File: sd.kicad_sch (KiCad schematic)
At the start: 40 parts, among them Y1 ABM8G-24.000MHZ-18-D2Y-T

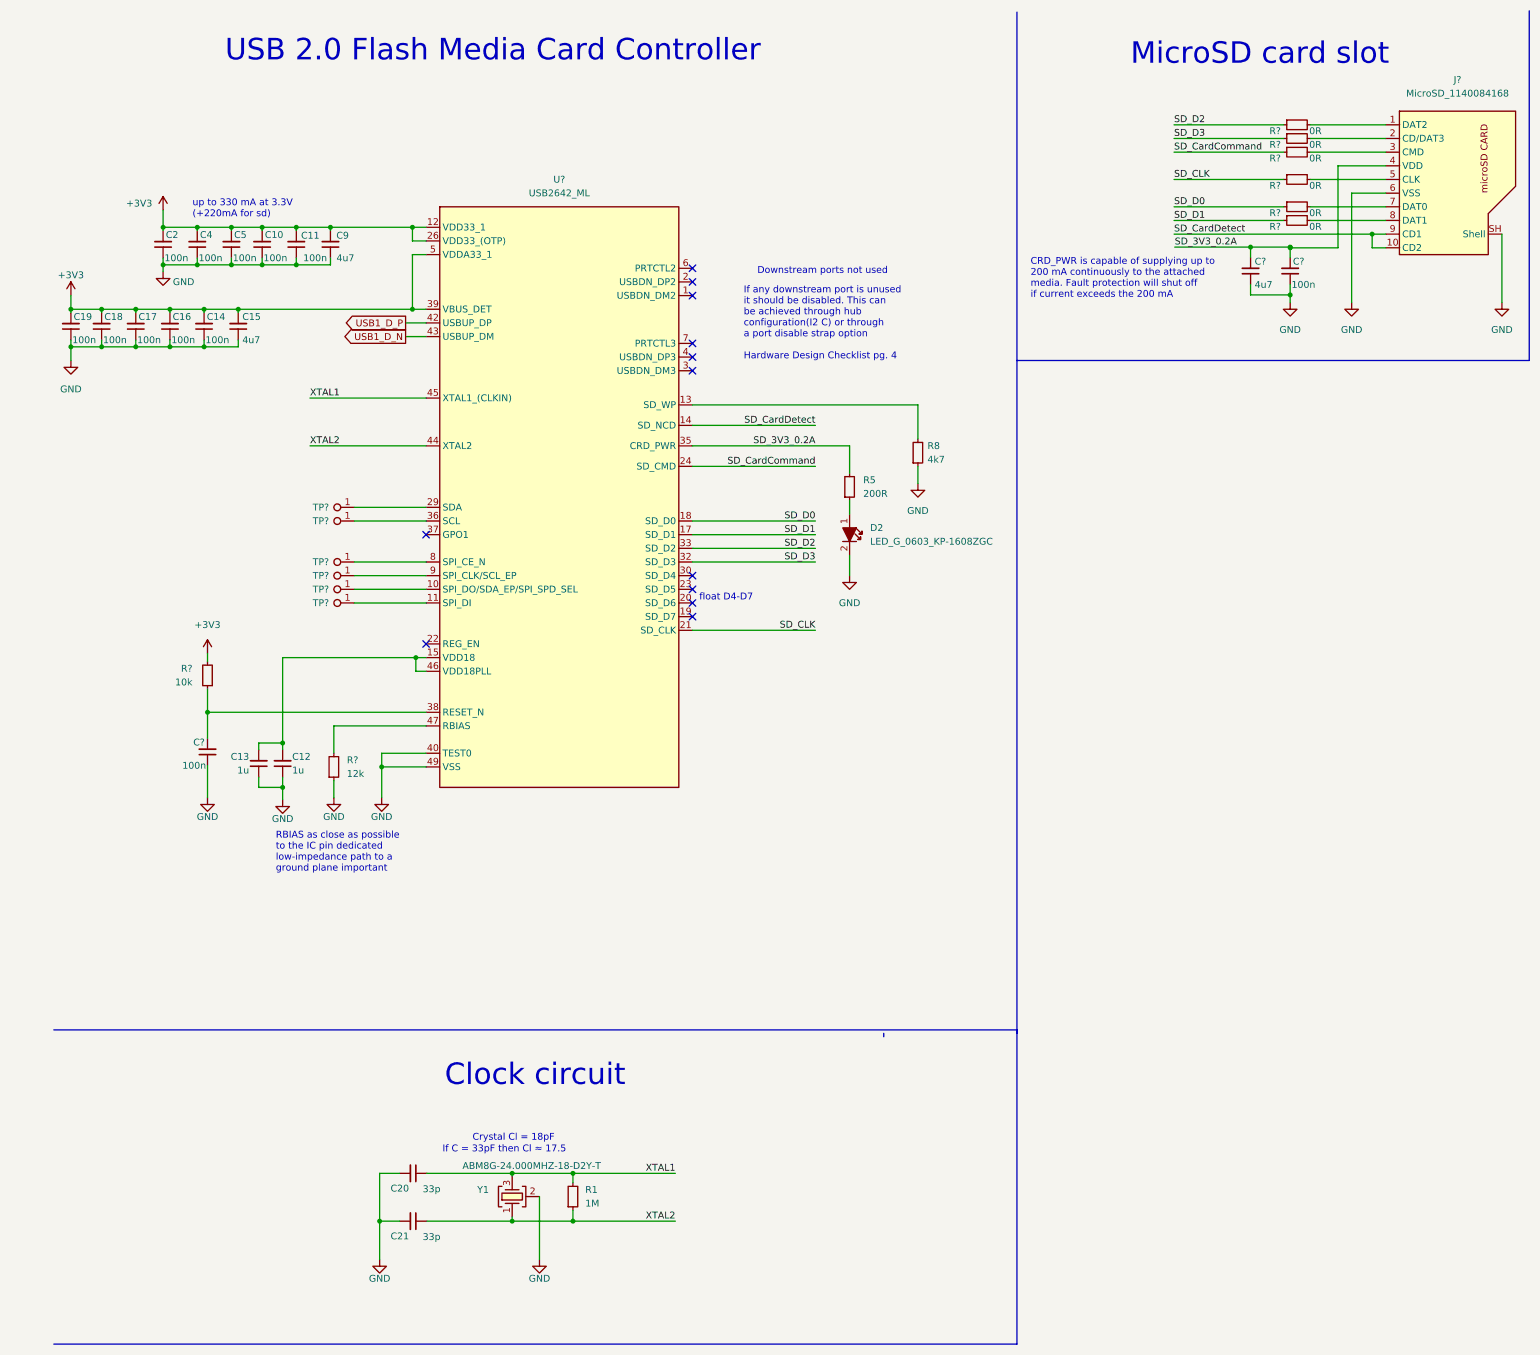
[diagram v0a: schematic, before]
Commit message: [#45990] Route dif Pcie, place susclk gen
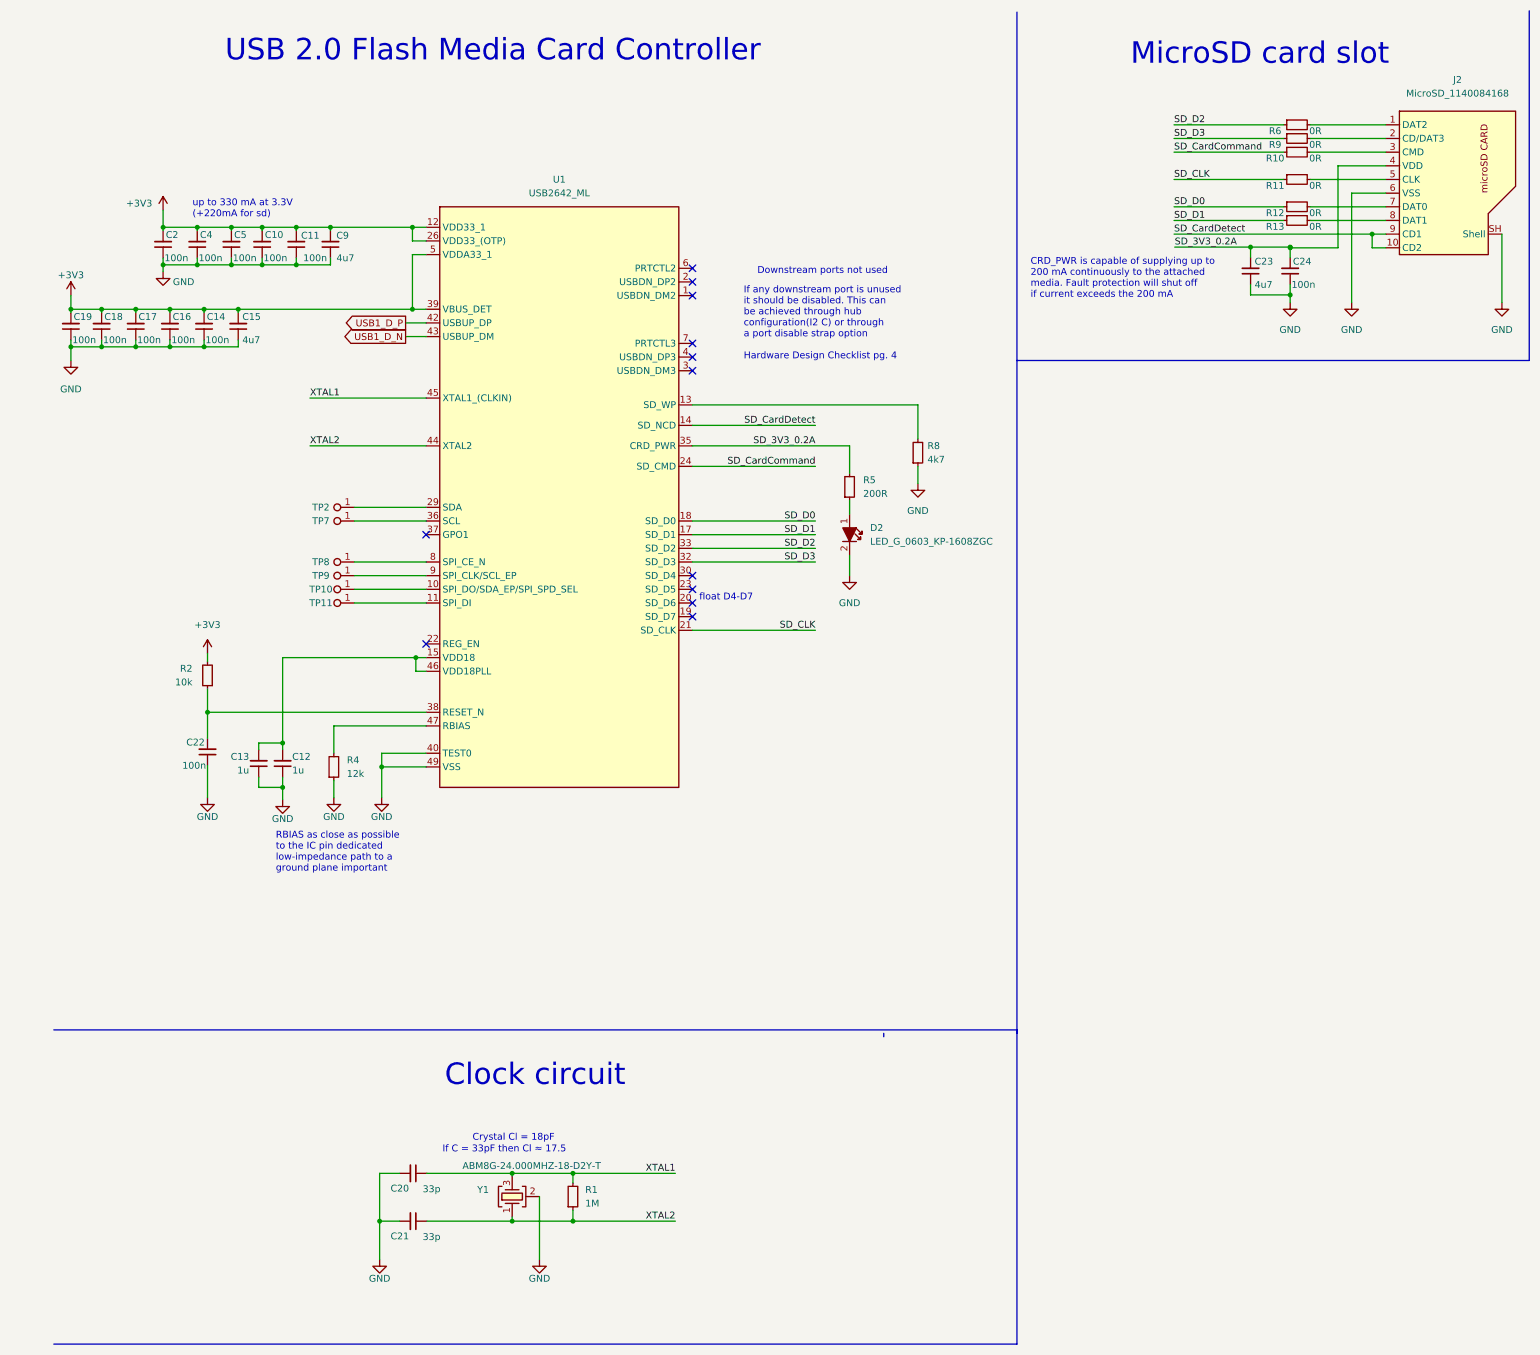
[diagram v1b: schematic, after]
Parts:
- gave numbers to parts that had none: 19
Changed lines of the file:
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@@
   (symbol (lib_id "antmicroResistors0603:R_0R_0603") (at 240.665 43.18 0) (unit 1)
     (in_bom yes) (on_board yes)
-    (property "Reference" "R?" (id 0) (at 239.141 44.323 0)
+    (property "Reference" "R11" (id 0) (at 239.141 44.323 0)
       (effects (font (size 1.27 1.27) (thickness 0.15)))
     )
@@
   (symbol (lib_id "antmicroResistors0402:R_10k_0402") (at 40.64 137.922 270) (mirror x) (unit 1)
     (in_bom yes) (on_board yes) (fields_autoplaced)
-    (property "Reference" "R?" (id 0) (at 37.846 134.1119 90)
+    (property "Reference" "R2" (id 0) (at 37.846 134.1119 90)
       (effects (font (size 1.27 1.27) (thickness 0.15)) (justify right))
     )
@@
   (symbol (lib_id "antmicroTestPoints:TP_0.75mm_SMD") (at 67.945 104.14 180) (unit 1)
     (in_bom yes) (on_board yes)
-    (property "Reference" "TP?" (id 0) (at 61.722 104.14 0)
+    (property "Reference" "TP2" (id 0) (at 61.722 104.14 0)
       (effects (font (size 1.27 1.27) (thickness 0.15)))
     )
@@
   (symbol (lib_id "antmicroTestPoints:TP_0.75mm_SMD") (at 67.945 114.3 180) (unit 1)
     (in_bom yes) (on_board yes)
-    (property "Reference" "TP?" (id 0) (at 61.722 114.3 0)
+    (property "Reference" "TP8" (id 0) (at 61.722 114.3 0)
       (effects (font (size 1.27 1.27) (thickness 0.15)))
     )
@@
   (symbol (lib_id "antmicroResistors0603:R_0R_0603") (at 240.665 35.56 0) (unit 1)
     (in_bom yes) (on_board yes)
-    (property "Reference" "R?" (id 0) (at 239.141 36.703 0)
+    (property "Reference" "R9" (id 0) (at 239.141 36.703 0)
       (effects (font (size 1.27 1.27) (thickness 0.15)))
     )
@@
   (symbol (lib_id "antmicroTestPoints:TP_0.75mm_SMD") (at 67.945 121.92 180) (unit 1)
     (in_bom yes) (on_board yes)
-    (property "Reference" "TP?" (id 0) (at 61.722 121.92 0)
+    (property "Reference" "TP11" (id 0) (at 61.722 121.92 0)
       (effects (font (size 1.27 1.27) (thickness 0.15)))
     )
@@
   (symbol (lib_id "antmicroCapacitors0402:C_100n_0402") (at 40.64 152.146 270) (mirror x) (unit 1)
     (in_bom yes) (on_board yes)
-    (property "Reference" "C?" (id 0) (at 40.132 147.828 90)
+    (property "Reference" "C22" (id 0) (at 40.132 147.828 90)
       (effects (font (size 1.27 1.27) (thickness 0.15)) (justify right))
     )
@@
   (symbol (lib_id "antmicroCapacitors0402:C_100n_0402") (at 241.935 62.738 90) (unit 1)
     (in_bom yes) (on_board yes)
-    (property "Reference" "C?" (id 0) (at 242.443 58.42 90)
+    (property "Reference" "C24" (id 0) (at 242.443 58.42 90)
       (effects (font (size 1.27 1.27) (thickness 0.15)) (justify right))
     )
@@
   (symbol (lib_id "antmicroResistors0603:R_0R_0603") (at 240.665 33.02 0) (unit 1)
     (in_bom yes) (on_board yes)
-    (property "Reference" "R?" (id 0) (at 239.141 34.163 0)
+    (property "Reference" "R6" (id 0) (at 239.141 34.163 0)
       (effects (font (size 1.27 1.27) (thickness 0.15)))
     )
@@
   (symbol (lib_id "antmicroTestPoints:TP_0.75mm_SMD") (at 67.945 106.68 180) (unit 1)
     (in_bom yes) (on_board yes)
-    (property "Reference" "TP?" (id 0) (at 61.722 106.68 0)
+    (property "Reference" "TP7" (id 0) (at 61.722 106.68 0)
       (effects (font (size 1.27 1.27) (thickness 0.15)))
     )
@@
   (symbol (lib_id "antmicropower:GND") (at 253.365 66.04 0) (unit 1)
     (in_bom yes) (on_board yes) (fields_autoplaced)
-    (property "Reference" "#PWR?" (id 0) (at 253.365 72.39 0)
+    (property "Reference" "#PWR0115" (id 0) (at 253.365 72.39 0)
       (effects (font (size 1.27 1.27)) hide)
     )
@@
   (symbol (lib_id "antmicropower:GND") (at 40.64 158.115 0) (mirror y) (unit 1)
     (in_bom yes) (on_board yes)
-    (property "Reference" "#PWR?" (id 0) (at 40.64 164.465 0)
+    (property "Reference" "#PWR0112" (id 0) (at 40.64 164.465 0)
       (effects (font (size 1.27 1.27)) hide)
     )
@@
   (symbol (lib_id "antmicroMemoryConnectorsPCCardSockets:MicroSD_1140084168") (at 259.715 33.02 0) (unit 1)
     (in_bom yes) (on_board yes) (fields_autoplaced)
-    (property "Reference" "J?" (id 0) (at 273.05 24.638 0)
+    (property "Reference" "J2" (id 0) (at 273.05 24.638 0)
       (effects (font (size 1.27 1.27) (thickness 0.15)))
     )
@@
   (symbol (lib_id "antmicroResistors0603:R_0R_0603") (at 240.665 48.26 0) (unit 1)
     (in_bom yes) (on_board yes)
-    (property "Reference" "R?" (id 0) (at 239.141 49.403 0)
+    (property "Reference" "R12" (id 0) (at 239.141 49.403 0)
       (effects (font (size 1.27 1.27) (thickness 0.15)))
     )
@@
   (symbol (lib_id "antmicroInterfaceControllers:USB2642_ML") (at 130.81 46.99 0) (unit 1)
     (in_bom yes) (on_board yes) (fields_autoplaced)
-    (property "Reference" "U?" (id 0) (at 106.045 43.18 0)
+    (property "Reference" "U1" (id 0) (at 106.045 43.18 0)
       (effects (font (size 1.27 1.27) (thickness 0.15)))
     )
@@
   (symbol (lib_id "antmicropower:+3V3") (at 40.64 131.318 0) (unit 1)
     (in_bom yes) (on_board yes) (fields_autoplaced)
-    (property "Reference" "#PWR?" (id 0) (at 40.64 135.128 0)
+    (property "Reference" "#PWR0113" (id 0) (at 40.64 135.128 0)
       (effects (font (size 1.27 1.27)) hide)
     )
@@
   (symbol (lib_id "antmicroTestPoints:TP_0.75mm_SMD") (at 67.945 119.38 180) (unit 1)
     (in_bom yes) (on_board yes)
-    (property "Reference" "TP?" (id 0) (at 61.722 119.38 0)
+    (property "Reference" "TP10" (id 0) (at 61.722 119.38 0)
       (effects (font (size 1.27 1.27) (thickness 0.15)))
     )
@@
   (symbol (lib_id "antmicroResistorsmisc:R_12k_0805") (at 64.135 154.94 90) (unit 1)
     (in_bom yes) (on_board yes) (fields_autoplaced)
-    (property "Reference" "R?" (id 0) (at 66.548 151.1299 90)
+    (property "Reference" "R4" (id 0) (at 66.548 151.1299 90)
       (effects (font (size 1.27 1.27) (thickness 0.15)) (justify right))
     )
@@
   (symbol (lib_id "antmicropower:GND") (at 241.935 66.04 0) (unit 1)
     (in_bom yes) (on_board yes) (fields_autoplaced)
-    (property "Reference" "#PWR?" (id 0) (at 241.935 72.39 0)
+    (property "Reference" "#PWR0117" (id 0) (at 241.935 72.39 0)
       (effects (font (size 1.27 1.27)) hide)
     )
@@
   (symbol (lib_id "antmicroResistors0603:R_0R_0603") (at 240.665 38.1 0) (unit 1)
     (in_bom yes) (on_board yes)
-    (property "Reference" "R?" (id 0) (at 239.141 39.243 0)
+    (property "Reference" "R10" (id 0) (at 239.141 39.243 0)
       (effects (font (size 1.27 1.27) (thickness 0.15)))
     )
@@
   (symbol (lib_id "antmicropower:GND") (at 64.135 158.115 0) (mirror y) (unit 1)
     (in_bom yes) (on_board yes)
-    (property "Reference" "#PWR?" (id 0) (at 64.135 164.465 0)
+    (property "Reference" "#PWR0109" (id 0) (at 64.135 164.465 0)
       (effects (font (size 1.27 1.27)) hide)
     )
@@
   (symbol (lib_id "antmicroCapacitors0402:C_4u7_0402") (at 234.569 62.738 90) (unit 1)
     (in_bom yes) (on_board yes)
-    (property "Reference" "C?" (id 0) (at 235.331 58.42 90)
+    (property "Reference" "C23" (id 0) (at 235.331 58.42 90)
       (effects (font (size 1.27 1.27) (thickness 0.15)) (justify right))
     )
@@
   (symbol (lib_id "antmicroTestPoints:TP_0.75mm_SMD") (at 67.945 116.84 180) (unit 1)
     (in_bom yes) (on_board yes)
-    (property "Reference" "TP?" (id 0) (at 61.722 116.84 0)
+    (property "Reference" "TP9" (id 0) (at 61.722 116.84 0)
       (effects (font (size 1.27 1.27) (thickness 0.15)))
     )
@@
   (symbol (lib_id "antmicroResistors0603:R_0R_0603") (at 240.665 50.8 0) (unit 1)
     (in_bom yes) (on_board yes)
-    (property "Reference" "R?" (id 0) (at 239.141 51.943 0)
-      (effects (font (size 1.27 1.27) (thickness 0.15)))
-    )
+    (property "Reference" "R13" (id 0) (at 239.141 51.943 0)
+      (effects (font (size 1.27 1.27) (thickness 0.15)))
+    )

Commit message: [#45990] Fix silk screen drcs
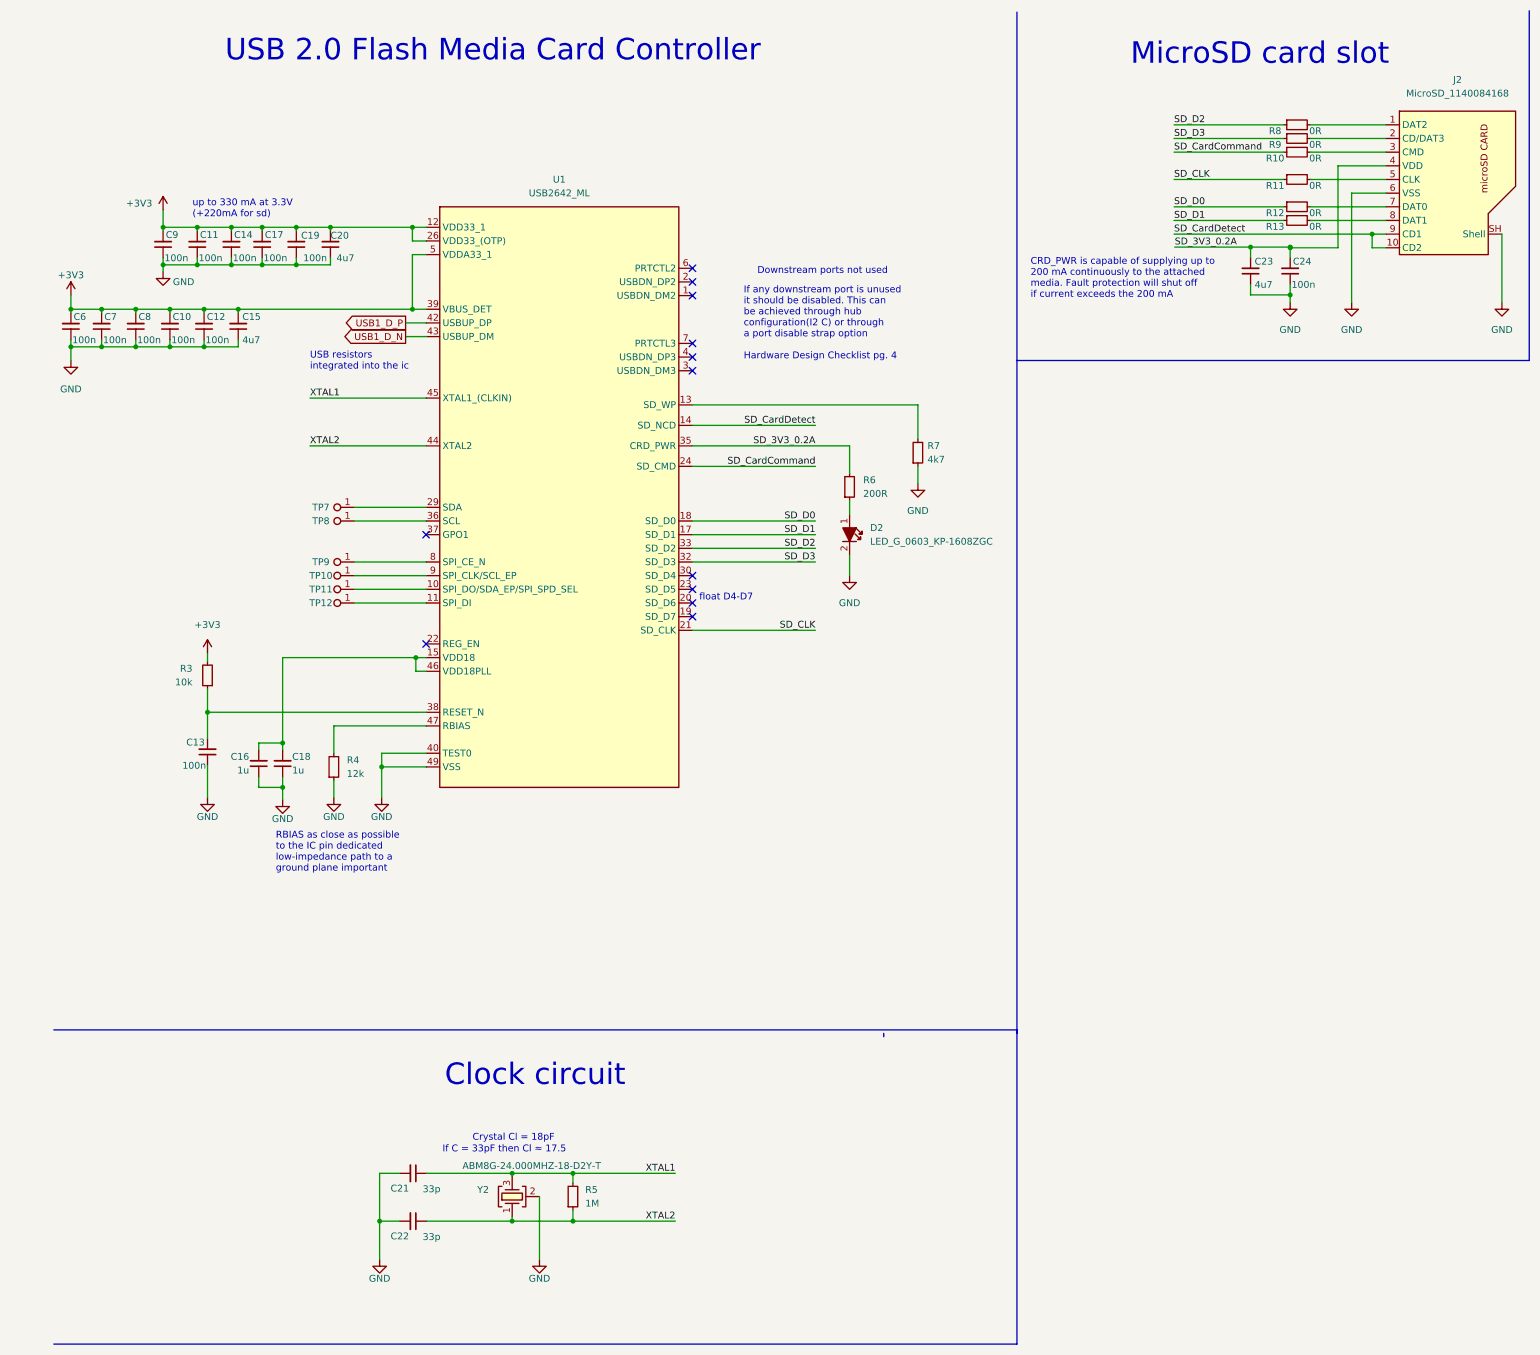
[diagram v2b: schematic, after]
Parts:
- renumbered C16 to C10, C4 to C11, C14 to C12, C22 to C13, C5 to C14, C13 to C16, C10 to C17, C12 to C18, C11 to C19, C9 to C20, C20 to C21, C21 to C22, C19 to C6, C18 to C7, C17 to C8, C2 to C9, R2 to R3, R1 to R5, R5 to R6, R8 to R7, R6 to R8, TP9 to TP10, TP10 to TP11, TP11 to TP12, TP2 to TP7, TP7 to TP8, TP8 to TP9, Y1 to Y2
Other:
- note added: "USB resistors integrated into the ic"
